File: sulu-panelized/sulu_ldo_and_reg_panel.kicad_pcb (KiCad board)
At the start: 2 copper layers, 41.7 x 73.2 mm, 108 parts, among them J1 Conn_02x11_Odd_Even, J10 through_hole, J11 through_hole, J12 through_hole, J13 through_hole, J14 through_hole, J15 through_hole, J16 through_hole, J17 through_hole, J18 through_hole, J19 through_hole, J2 Conn_02x10_Odd_Even, J20 through_hole, J21 through_hole, J3 Conn_02x05_Odd_Even, J4 Conn_01x01_Male, J5 through_hole, J6 through_hole, J7 through_hole, J8 through_hole, J9 through_hole, U1 scum3, U2 LP5907MFX-1.8, U2 S-85S1AB18-I6T1U, U3 S-85S1AB11-I6T1U, U3 TLV70311DBVR, U9AB1 ICM-20948

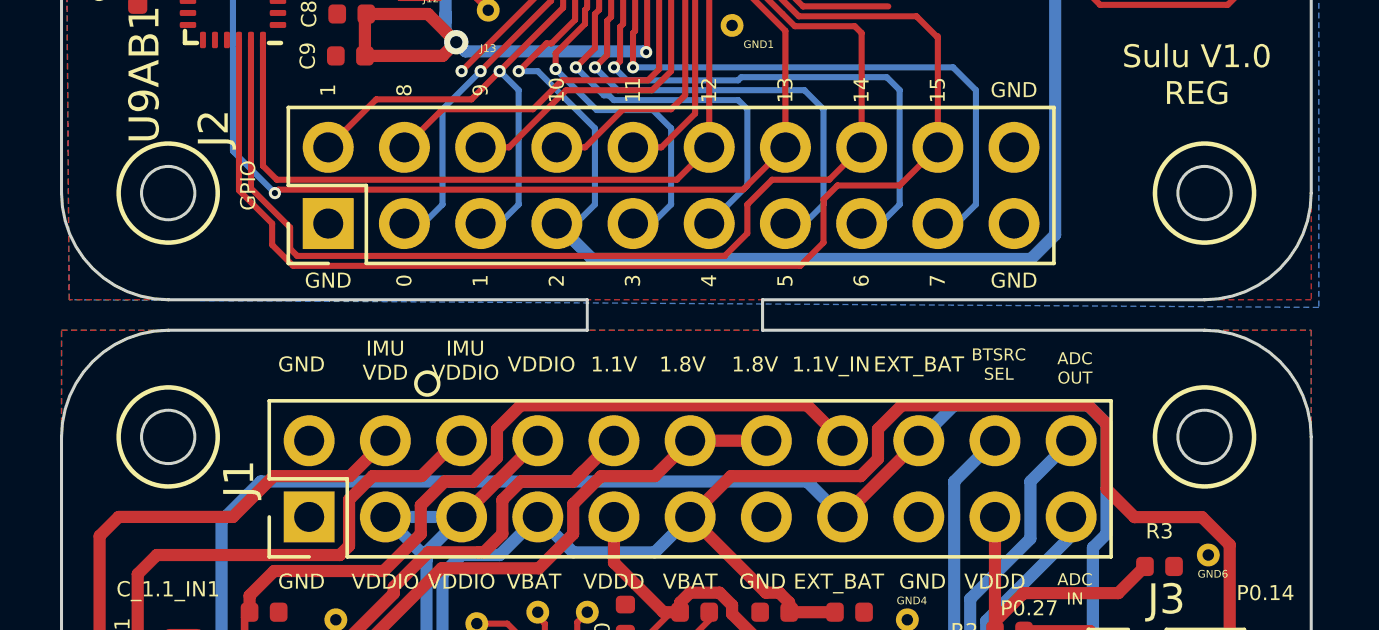
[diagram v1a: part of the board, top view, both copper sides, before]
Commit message: removed tab to separate panels
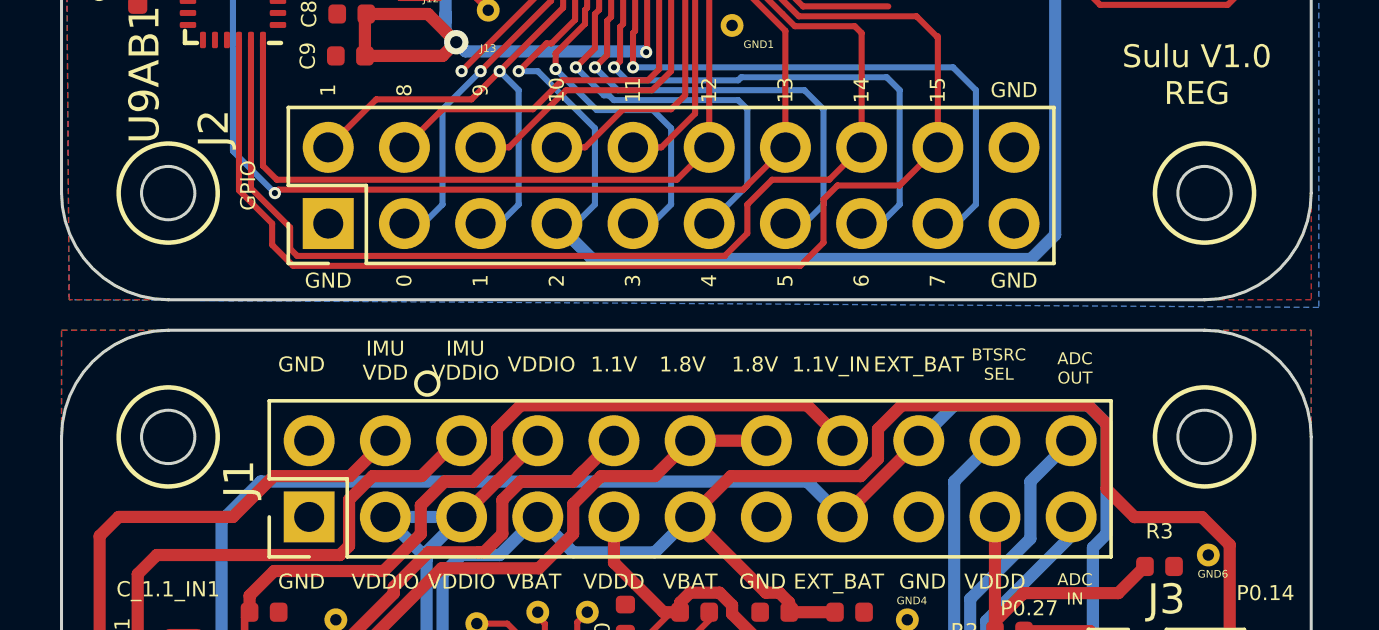
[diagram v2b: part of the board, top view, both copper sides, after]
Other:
- outline, holes or cut-outs redrawn
